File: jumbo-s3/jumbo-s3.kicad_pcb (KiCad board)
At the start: 2 copper layers, 26 parts, among them J1 GPIO, U1 ESP32-S3, U2 APS12808L-3OBM-BA, U3 W25Q128JVS, Y1 40MHz 10ppm

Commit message: pcb: rev. 1
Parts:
- removed U3: W25Q128JVS, Package_SO:SOIC-8_5.23x5.23mm_P1.27mm
- added J2: GPIO, Connector_PinSocket_2.54mm:PinSocket_1x12_P2.54mm_Vertical, F.Cu at (149.0, 116.5)
- C9, R1: moved to B.Cu
- J1: value GPIO -> UART; footprint Connector_PinHeader_2.54mm:PinHeader_2x10_P2.54mm_Vertical_SMD -> Connector_PinHeader_2.54mm:PinHeader_1x04_P2.54mm_Vertical; moved to B.Cu
- moved C10 69.8 mm to (171.6, 134.3), turned to 90 degrees
- moved L2 67.8 mm to (174.2, 130.5)
- moved L1 62.5 mm to (173.3, 126.2), turned to -90 degrees
- moved J1 60.2 mm to (160.8, 138.3), turned to 90 degrees
- moved AE1 59.4 mm to (179.2, 130.7), turned to -90 degrees
- moved C12 56.2 mm to (175.2, 133.1), turned to -90 degrees
- moved R1 53.2 mm to (173.3, 132.5), turned to 90 degrees
- moved Y1 52.6 mm to (167.8, 134.8), turned to 180 degrees
- moved C15 50.9 mm to (173.3, 133.1), turned to 90 degrees
- moved C2 48.5 mm to (175.1, 126.2), turned to 90 degrees
- moved C7 48.1 mm to (174.2, 123.5)
- moved C9 47.3 mm to (171.7, 132.5), turned to -90 degrees
- moved R3 46.3 mm to (164.0, 134.7), turned to 90 degrees
- moved C14 45.9 mm to (169.7, 138.3)
- moved C8 43.0 mm to (164.5, 120.9)
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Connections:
- C3 pad 1: Net-(C3-Pad1) -> VDD3P3
- J1 pad 1: +3V3 -> +3.3V
- J1 pad 2: EN -> TxD
- J1 pad 3: GPIO0 -> RxD
- J1 pad 4: GPIO1 -> GND
- L1 pad 2: Net-(C3-Pad1) -> VDD3P3
- U1 pad 10: GPIO5 -> unconnected-(U1-Pad10)
- U1 pad 11: GPIO6 -> unconnected-(U1-Pad11)
- U1 pad 12: GPIO7 -> unconnected-(U1-Pad12)
- U1 pad 13: GPIO8 -> unconnected-(U1-Pad13)
- U1 pad 14: GPIO9 -> unconnected-(U1-Pad14)
- U1 pad 22: GPIO16 -> unconnected-(U1-Pad22)
- U1 pad 23: GPIO17 -> unconnected-(U1-Pad23)
- U1 pad 24: GPIO18 -> unconnected-(U1-Pad24)
- U1 pad 27: GPIO21 -> unconnected-(U1-Pad27)
- U1 pad 32: SPICS0 -> unconnected-(U1-Pad32)
- U1 pad 36: GPIO48 -> unconnected-(U1-Pad36)
- U1 pad 37: GPIO47 -> unconnected-(U1-Pad37)
- U1 pad 43: GPIO38 -> unconnected-(U1-Pad43)
- U1 pad 44: GPIO39 -> unconnected-(U1-Pad44)
- U1 pad 45: GPIO40 -> unconnected-(U1-Pad45)
- U1 pad 47: GPIO41 -> unconnected-(U1-Pad47)
- U1 pad 48: GPIO42 -> unconnected-(U1-Pad48)
- U1 pad 51: GPIO45 -> unconnected-(U1-Pad51)
- U1 pad 52: GPIO46 -> unconnected-(U1-Pad52)
- U1 pad 6: GPIO1 -> unconnected-(U1-Pad6)
- U1 pad 7: GPIO2 -> unconnected-(U1-Pad7)
- U1 pad 8: GPIO3 -> unconnected-(U1-Pad8)
- U1 pad 9: GPIO4 -> unconnected-(U1-Pad9)
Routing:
- net +3.3V: track 0.00 -> 73.7 mm, vias 0 -> 3
- net GND: track 0.00 -> 42.0 mm, vias 0 -> 120
- net VDD_SPI: track 0.00 -> 41.9 mm, vias 0 -> 5
- net EN: track 0.00 -> 21.1 mm, vias 0 -> 1
- net GPIO20: track 0.00 -> 19.4 mm, vias 0 -> 1
- net GPIO19: track 0.00 -> 17.7 mm, vias 0 -> 1
- net SPI_DQS: track 0.00 -> 17.6 mm
- net SPI_IO6: track 0.00 -> 17.5 mm
- net SPICLK: track 0.00 -> 17.5 mm
- net SPICS1: track 0.00 -> 17.5 mm
- net SPI_IO5: track 0.00 -> 17.4 mm
- net SPIQ: track 0.00 -> 17.4 mm
- net SPID: track 0.00 -> 17.4 mm
- net GPIO14: track 0.00 -> 17.1 mm
- net SPI_IO7: track 0.00 -> 16.9 mm, vias 0 -> 2
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- added copper zone on B.Cu, net GND
- added copper zone on F.Cu, net GND
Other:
- board outline added: 40.5 x 27.3 mm
- board text added: "Designed by Jackson M Hu"
- board text added: "EN 0 10 11 12 13 VCC GND 14 15 19 20"
- board text added: "GND RxD TxD 3V3"
- board text added: "Jumbo ESP32 ESP32S3 & APS12808"
- board text added: "Rev. 1 Sep 2022"

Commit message: Rev 2: init
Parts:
- removed J2: GPIO, Connector_PinSocket_2.54mm:PinSocket_1x12_P2.54mm_Vertical
- C9, R1: moved to F.Cu
- J1: value UART -> GPIO; footprint Connector_PinHeader_2.54mm:PinHeader_1x04_P2.54mm_Vertical -> Connector_PinHeader_1.27mm:PinHeader_2x15_P1.27mm_Vertical_SMD
- moved J1 20.3 mm to (168.2, 119.5)
- moved R1 19.5 mm to (154.8, 138.7), turned to 0 degrees
- moved C9 14.6 mm to (158.4, 138.7), turned to 0 degrees
- moved C4 0.53 mm to (168.6, 120.8)
- moved C8 0.10 mm to (164.4, 120.8)
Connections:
- J1 pad 2: TxD -> +3.3V
- J1 pad 3: RxD -> GPIO0
- J1 pad 4: GND -> GPIO10
- U1 pad 10: unconnected-(U1-Pad10) -> GPIO5
- U1 pad 11: unconnected-(U1-Pad11) -> GPIO6
- U1 pad 12: unconnected-(U1-Pad12) -> GPIO7
- U1 pad 13: unconnected-(U1-Pad13) -> GPIO8
- U1 pad 14: unconnected-(U1-Pad14) -> GPIO9
- U1 pad 22: unconnected-(U1-Pad22) -> GPIO16
- U1 pad 23: unconnected-(U1-Pad23) -> GPIO17
- U1 pad 24: unconnected-(U1-Pad24) -> GPIO18
- U1 pad 27: unconnected-(U1-Pad27) -> GPIO21
- U1 pad 6: unconnected-(U1-Pad6) -> GPIO1
- U1 pad 7: unconnected-(U1-Pad7) -> GPIO2
- U1 pad 8: unconnected-(U1-Pad8) -> GPIO3
- U1 pad 9: unconnected-(U1-Pad9) -> GPIO4
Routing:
- net +3.3V: track 73.7 -> 15.2 mm, vias 3 -> 14
- net GPIO6: track 0.00 -> 14.9 mm, vias 0 -> 2
- net GPIO4: track 0.00 -> 14.6 mm, vias 0 -> 2
- net GPIO5: track 0.00 -> 14.0 mm, vias 0 -> 2
- net GPIO7: track 0.00 -> 13.2 mm, vias 0 -> 2
- net RxD: track 14.4 -> 1.18 mm
- net GPIO20: track 19.4 -> 8.98 mm
- net GPIO15: track 16.8 -> 6.73 mm
- net GPIO8: track 0.00 -> 9.79 mm, vias 0 -> 2
- net GPIO1: track 0.00 -> 9.67 mm, vias 0 -> 1
- net GPIO21: track 0.00 -> 9.65 mm, vias 0 -> 1
- net TxD: track 9.37 -> 0.00 mm
- net GPIO19: track 17.7 -> 8.34 mm
- net GPIO14: track 17.1 -> 8.02 mm, vias 0 -> 1
- net GPIO18: track 0.00 -> 8.64 mm, vias 0 -> 1
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- added copper zone on In2.Cu, net +3.3V
- added copper zone on In1.Cu, net GND
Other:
- board size 40.5 x 27.3 mm -> 38 x 25 mm
- copper layers 2 -> 4
- board text removed: "EN 0 10 11 12 13 VCC GND 14 15 19 20"
- board text removed: "GND RxD TxD 3V3"

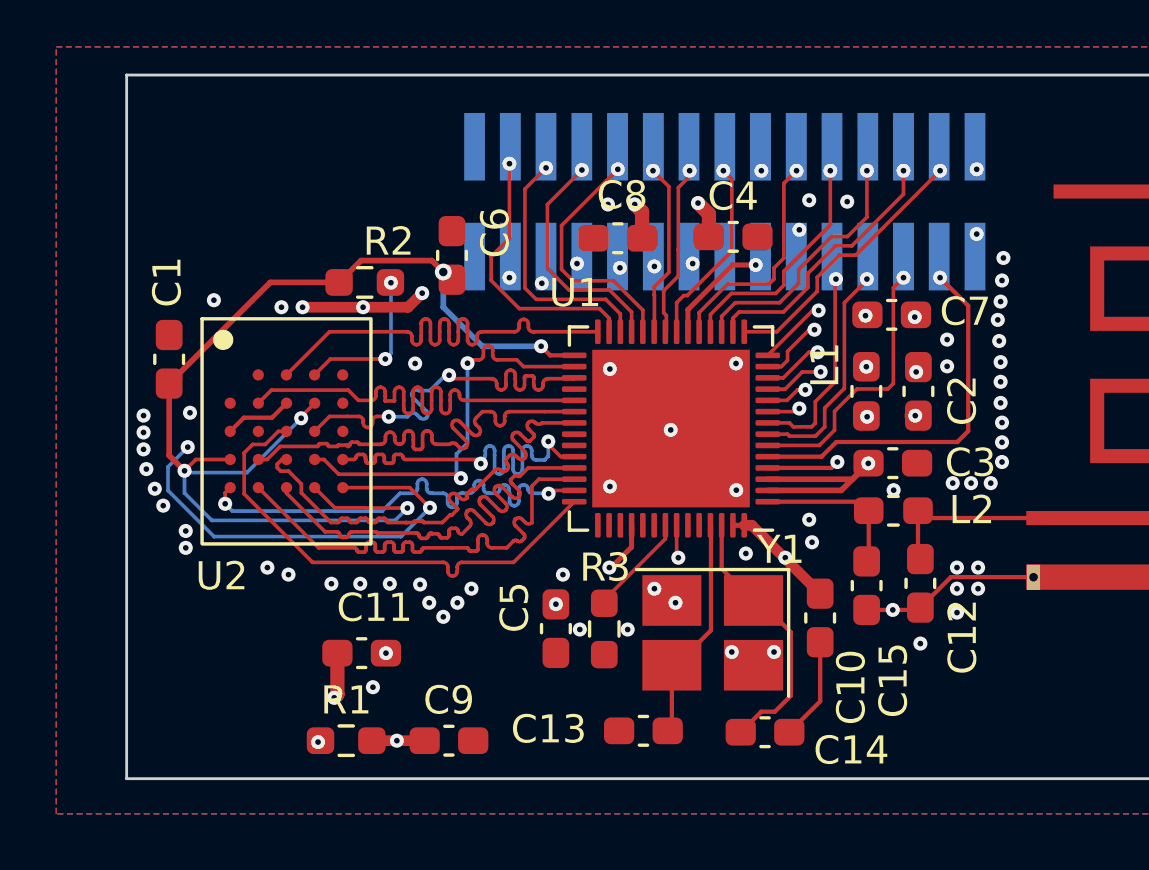
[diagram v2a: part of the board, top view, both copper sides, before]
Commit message: rev2: pcb: connect everything up
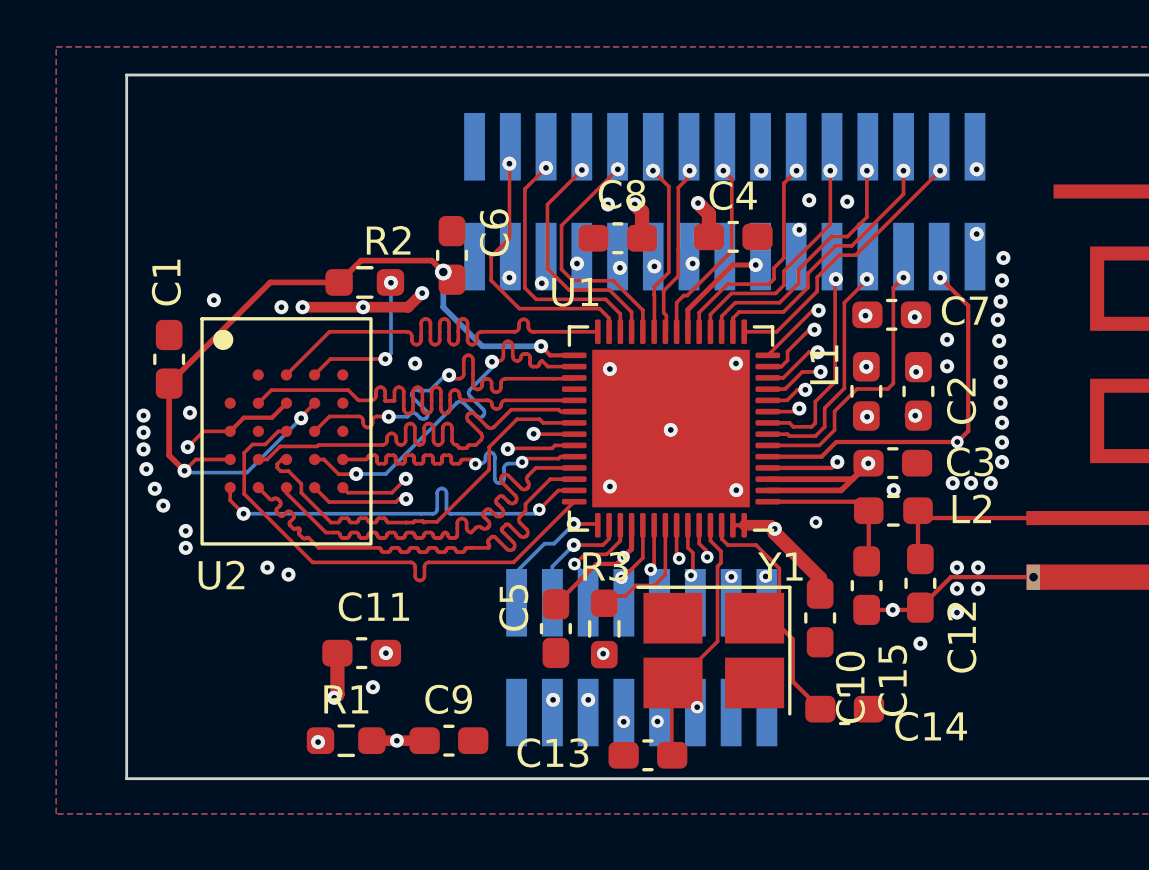
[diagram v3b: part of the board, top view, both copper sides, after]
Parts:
- added J2: DEBUG, Connector_PinHeader_1.27mm:PinHeader_2x08_P1.27mm_Vertical_SMD, B.Cu at (165.3, 135.7)
- moved C14 2.95 mm to (172.5, 137.5)
- moved C13 0.88 mm to (165.5, 139.2)
- moved Y1 0.63 mm to (167.9, 135.4)
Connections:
- U1 pad 36: unconnected-(U1-Pad36) -> GPIO48
- U1 pad 37: unconnected-(U1-Pad37) -> GPIO47
- U1 pad 43: unconnected-(U1-Pad43) -> GPIO38
- U1 pad 44: unconnected-(U1-Pad44) -> GPIO39
- U1 pad 45: unconnected-(U1-Pad45) -> GPIO40
- U1 pad 47: unconnected-(U1-Pad47) -> GPIO41
- U1 pad 48: unconnected-(U1-Pad48) -> GPIO42
- U1 pad 51: unconnected-(U1-Pad51) -> GPIO45
- U1 pad 52: unconnected-(U1-Pad52) -> GPIO46
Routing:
- net GPIO0: track 13.4 -> 29.4 mm, vias 1 -> 3
- net GPIO47: track 0.00 -> 15.1 mm, vias 0 -> 2
- net GND: track 34.2 -> 19.2 mm, vias 74 -> 57
- net GPIO48: track 0.00 -> 11.2 mm, vias 0 -> 2
- net RxD: track 1.18 -> 6.02 mm, vias 1 -> 2
- net GPIO38: track 0.00 -> 4.71 mm, vias 0 -> 1
- net GPIO39: track 0.00 -> 4.19 mm, vias 0 -> 1
- net TxD: track 0.00 -> 4.13 mm, vias 0 -> 2
- net GPIO40: track 0.00 -> 4.10 mm, vias 0 -> 1
- net GPIO42: track 0.00 -> 2.93 mm, vias 0 -> 1
- net SPID: track 17.4 -> 14.7 mm
- net XTAL_N: track 8.04 -> 10.5 mm
- net GPIO46: track 0.00 -> 2.40 mm, vias 0 -> 2
- net +3.3V: track 15.2 -> 17.4 mm, vias 14 -> 13
- net SPI_IO7: track 16.9 -> 14.7 mm
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
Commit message: rev2: finalise PCB
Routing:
- net SPID: track 14.7 -> 17.9 mm
- net SPI_IO4: track 12.4 -> 14.7 mm
- net +3.3V: track 17.4 -> 18.7 mm, vias 13 -> 15
- net RxD: track 6.02 -> 5.00 mm
- net VDD_SPI: track 41.4 -> 40.8 mm, vias 5 -> 7
- net GND: track 19.2 -> 19.0 mm, vias 57 -> 72
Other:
- board text added: "Rev. 2 Sep 2022"
- board text removed: "Rev. 1 Sep 2022"

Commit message: rev2: pcb: final adjustments
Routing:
- net +3.3V: track 18.7 -> 21.3 mm, vias 15 -> 14
- net XTAL_P: track 9.66 -> 8.34 mm
